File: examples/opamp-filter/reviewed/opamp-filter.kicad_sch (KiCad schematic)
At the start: 28 parts, among them J1 IN, J2 5V, J3 OUT, U1 MCP6001R, U2 MCP6001R

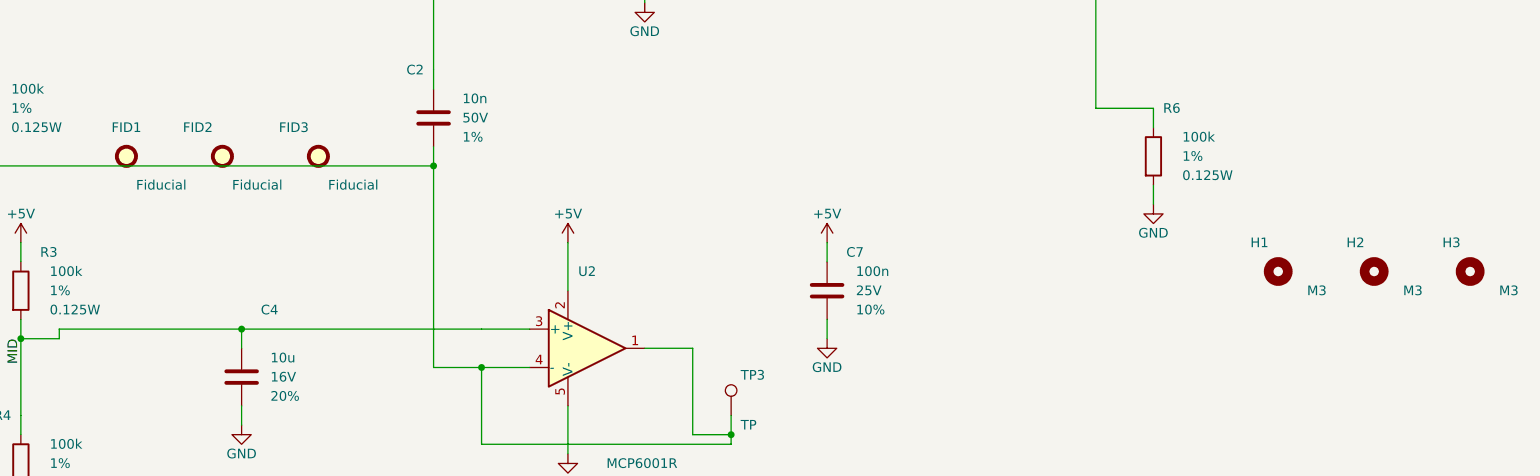
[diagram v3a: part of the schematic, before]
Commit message: Put the vias back where the copper moved, and let the fillets vote
The FPGA board came back from its re-route with two unconnected nets and
three dangling ends, and the cause was older than anything this round
added. The router hands back a via for every layer change; six passes
then reshape the copper - snapping to 45s, chamfering, spreading folds,
and now filleting - and none of them move the holes underneath. A joint
that slides a millimetre from its via is two loose ends and one broken
net, and `_unlooped` then swept the via away as orphaned, because it
kept a via only when a track ended on its exact coordinate.

Two fixes, both about what "connected" means. A via lives if kept copper
*touches* it, not if a coordinate matches. And a new `_joined` pass
re-derives the joints from the copper that actually got written: where a
net ends on two layers at one point with no via reaching it, one goes
back in. It reads the finished geometry, so it cannot drift the way six
separate passes carrying vias along with them would.

The same reasoning fixes two rules that had been measuring coordinates
rather than copper. `route.stub` matched a track end to a via's centre
exactly, and called a joint a stub whenever a reshaping pass had moved
it a quarter of a millimetre inside the very barrel it was connected to.
`route.width_step` walked a neck back to its pad and stopped at the
first width change - which, on a filleted board, is the teardrop, so
every escape's neck stopped being recognised as one.

While the three copies of the post-route pipeline were being edited for
the third time this session, they became one function. That is how
`_teardrops` had come to run on two of the three exits.

All five boards: DRC clean on both matrix versions, nothing unconnected.
Four pass their gates; the FPGA board is down to the two-layer bill it
has always had - four nets over plane cuts and one 88 degree corner.

Co-Authored-By: Claude Fable 5 <noreply@anthropic.com>
Claude-Session: https:/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
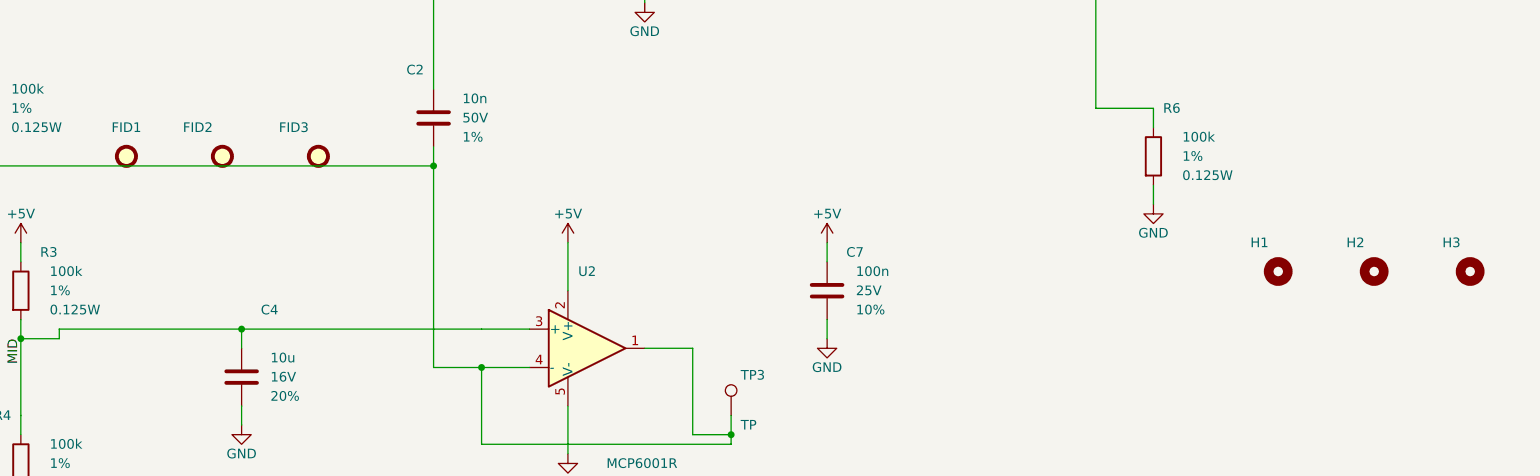
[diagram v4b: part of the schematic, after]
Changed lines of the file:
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@@
     (exclude_from_sim no) (in_bom no) (on_board yes) (dnp no)
     (property "Reference" "H1" (at 240.03 146.05 0) (effects (font (size 1.27 1.27)) (justify right)))
-    (property "Value" "M3" (at 245.11 152.4 0) (effects (font (size 1.27 1.27)) (justify left)))
+    (property "Value" "M3" (at 245.11 152.4 0) (effects (font (size 1.27 1.27)) (justify left) hide))
     (property "Footprint" "MountingHole:MountingHole_3.2mm_M3" (at 241.3 149.86 0) (effects (font (size 1.27 1.27)) hide))
     (property "Datasheet" "~" (at 241.3 149.86 0) (effects (font (size 1.27 1.27)) hide))
@@
     (exclude_from_sim no) (in_bom no) (on_board yes) (dnp no)
     (property "Reference" "H2" (at 252.73 146.05 0) (effects (font (size 1.27 1.27)) (justify right)))
-    (property "Value" "M3" (at 257.81 152.4 0) (effects (font (size 1.27 1.27)) (justify left)))
+    (property "Value" "M3" (at 257.81 152.4 0) (effects (font (size 1.27 1.27)) (justify left) hide))
     (property "Footprint" "MountingHole:MountingHole_3.2mm_M3" (at 254.0 149.86 0) (effects (font (size 1.27 1.27)) hide))
     (property "Datasheet" "~" (at 254.0 149.86 0) (effects (font (size 1.27 1.27)) hide))
@@
     (exclude_from_sim no) (in_bom no) (on_board yes) (dnp no)
     (property "Reference" "H3" (at 265.43 146.05 0) (effects (font (size 1.27 1.27)) (justify right)))
-    (property "Value" "M3" (at 270.51 152.4 0) (effects (font (size 1.27 1.27)) (justify left)))
+    (property "Value" "M3" (at 270.51 152.4 0) (effects (font (size 1.27 1.27)) (justify left) hide))
     (property "Footprint" "MountingHole:MountingHole_3.2mm_M3" (at 266.7 149.86 0) (effects (font (size 1.27 1.27)) hide))
     (property "Datasheet" "~" (at 266.7 149.86 0) (effects (font (size 1.27 1.27)) hide))
@@
     (exclude_from_sim no) (in_bom no) (on_board yes) (dnp no)
     (property "Reference" "FID1" (at 88.9 130.81 0) (effects (font (size 1.27 1.27))))
-    (property "Value" "Fiducial" (at 90.17 138.43 0) (effects (font (size 1.27 1.27)) (justify left)))
+    (property "Value" "Fiducial" (at 90.17 138.43 0) (effects (font (size 1.27 1.27)) (justify left) hide))
     (property "Footprint" "Fiducial:Fiducial_1mm_Mask2mm" (at 88.9 134.62 0) (effects (font (size 1.27 1.27)) hide))
     (property "Datasheet" "~" (at 88.9 134.62 0) (effects (font (size 1.27 1.27)) hide))
@@
     (exclude_from_sim no) (in_bom no) (on_board yes) (dnp no)
     (property "Reference" "FID2" (at 100.33 130.81 0) (effects (font (size 1.27 1.27)) (justify right)))
-    (property "Value" "Fiducial" (at 102.87 138.43 0) (effects (font (size 1.27 1.27)) (justify left)))
+    (property "Value" "Fiducial" (at 102.87 138.43 0) (effects (font (size 1.27 1.27)) (justify left) hide))
     (property "Footprint" "Fiducial:Fiducial_1mm_Mask2mm" (at 101.60000000000001 134.62 0) (effects (font (size 1.27 1.27)) hide))
     (property "Datasheet" "~" (at 101.60000000000001 134.62 0) (effects (font (size 1.27 1.27)) hide))
@@
     (exclude_from_sim no) (in_bom no) (on_board yes) (dnp no)
     (property "Reference" "FID3" (at 113.03 130.81 0) (effects (font (size 1.27 1.27)) (justify right)))
-    (property "Value" "Fiducial" (at 115.57 138.43 0) (effects (font (size 1.27 1.27)) (justify left)))
+    (property "Value" "Fiducial" (at 115.57 138.43 0) (effects (font (size 1.27 1.27)) (justify left) hide))
     (property "Footprint" "Fiducial:Fiducial_1mm_Mask2mm" (at 114.30000000000001 134.62 0) (effects (font (size 1.27 1.27)) hide))
     (property "Datasheet" "~" (at 114.30000000000001 134.62 0) (effects (font (size 1.27 1.27)) hide))

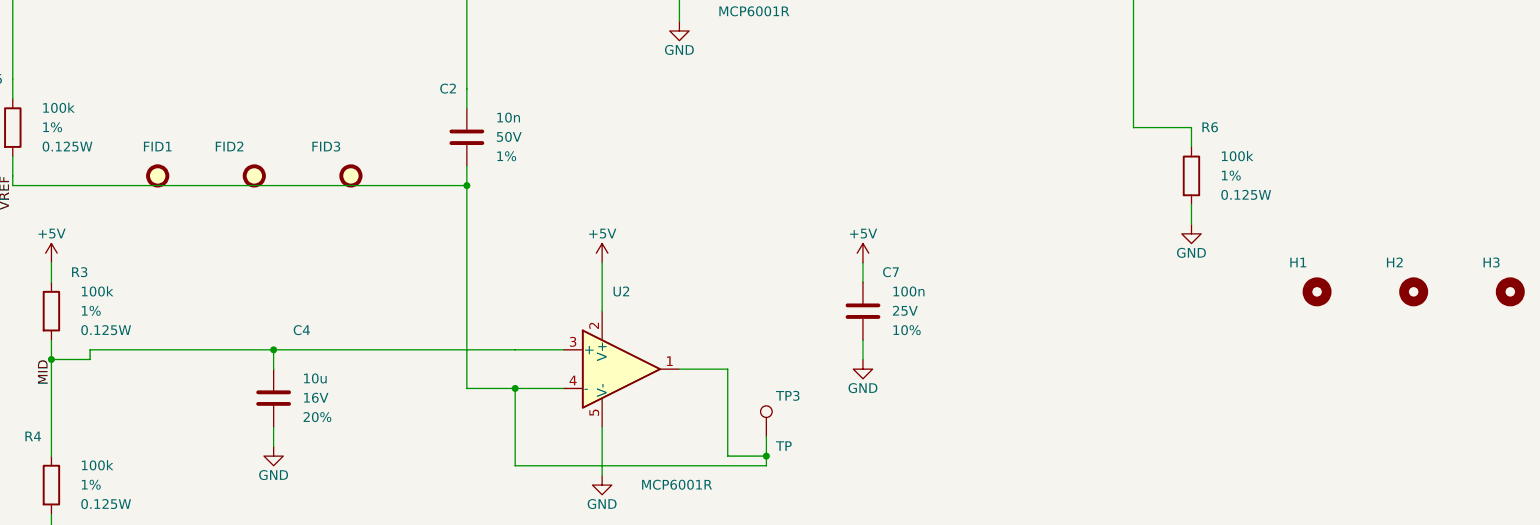
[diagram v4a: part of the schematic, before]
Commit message: Leave room for the screw, and print the ink where the board is
The screw holes were placed against the hole's own courtyard, which is the
drill plus a whisker - so on four of the five boards a hole sat inside a
connector's mating space, closest 0.42 mm. What goes through an M3 hole is a
pan head on a washer, seven millimetres of steel lying flat, and a connector
wants its shell, its wires and the fingers that fit them on top of that. The
spot search now keeps the fastener's own circle clear of every part body and
gives connectors CONNECTOR_ACCESS more, and three rules say so when a board
does not: mechanical.fastener_clearance, mechanical.connector_access and
mechanical.fastener_copper, all blocking for a generated design.

Silk was measured with a per-character advance of 0.78, and KiCad's stroke
font is proportional at 0.94 to 1.07. Everything downstream of that estimate
was placing ink where it did not fit: a legend across a capacitor's land, a
designator through the board's own name. `_text_extent` takes the top of the
measured range, adds the fab's clearance and is used by every silk placement.

Three placements also fell through to a position nobody chose. A designator
that found nothing kept its library offset, which for a part in a corner
points off the board; the board id took the first of eight fixed strips; a
legend took the least bad of six spots. All three are scored now, over
candidate sets wide enough to have an answer - and a pad-less footprint, which
is what a mounting hole is, is no longer skipped outright.

silk.off_board reports the case KiCad's own test cannot: ink that clears the
edge entirely is never printed, and DRC only measures ink that crosses it.

_unspiked redraws a corner tighter than a right angle as the elbow between its
neighbours - one diagonal, one straight, no step back to a heading the line
has already left. It is never longer than what it replaces.

All four fast boards: 0 errors, 0 warnings.

Co-Authored-By: Claude Fable 5 <no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
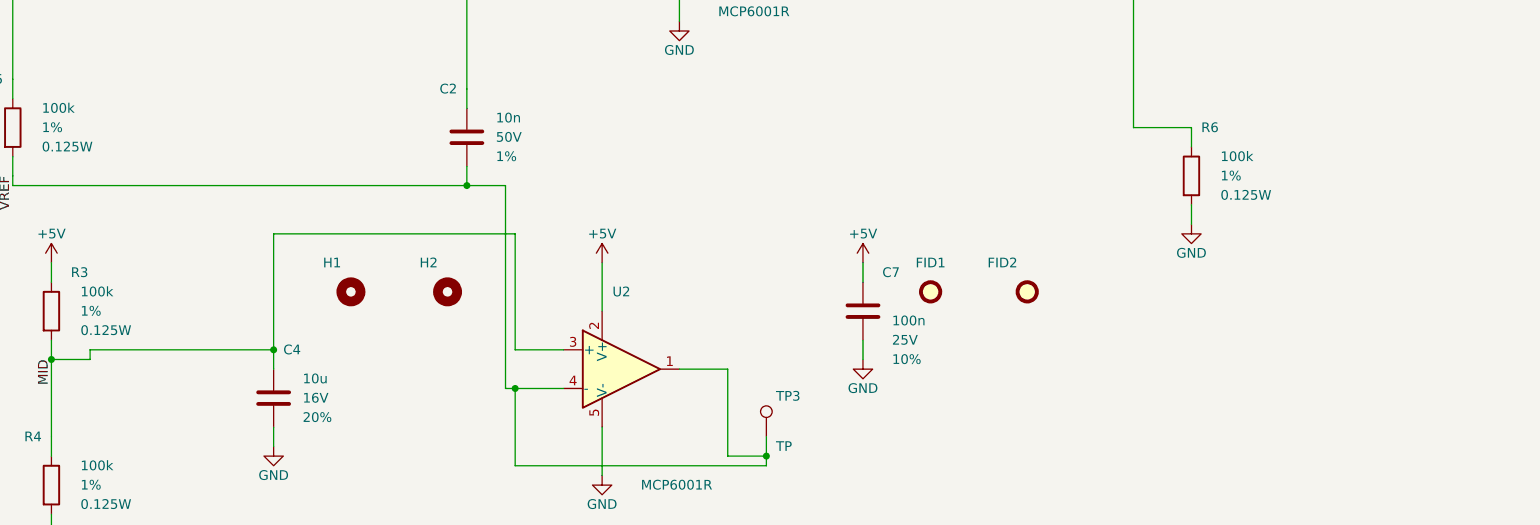
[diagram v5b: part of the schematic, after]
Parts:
- removed FID3: Fiducial, Fiducial:Fiducial_1mm_Mask2mm, symbol Mechanical:Fiducial
- removed H3: M3, MountingHole:MountingHole_3.2mm_M3, symbol Mechanical:MountingHole
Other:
- moved on the sheet: FID1, FID2, H1, H2

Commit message: Walk the whole edge for a screw hole, and land a joint on its own pad
The fastener clearance was right and the search was not: it slid along two
edges from each corner and gave up, so boards that had had four screw holes
came back with one. It now walks a ring round the board at the inset the
screw needs, taking the nearest free point to each corner - and only from
that corner's own quarter, because a search that asked for the nearest free
point anywhere put three of the four along one edge, each of them the nearest
thing to a different corner. A quarter with no room gives no screw: three
that hold the board flat beat four that hold one side.

A pin header asks for nothing above its courtyard - the socket that fits it
lands inside the outline the header already draws - while a screw terminal's
wires leave horizontally from its face. Treating the two alike is what left a
carrier lined with headers with two holes on one edge. Both the generator and
the rule now tell them apart by footprint.

_landed folds a via that sits beside a plated hole of its own net onto the
hole. The plating already joins the faces, so the via bought nothing and cost
hole-to-hole: two drills a millimetre apart leave 0.15 mm of laminate at a
0.25 mm rule, which is what DRC reported on the opamp board.

The fillets move to the end of the pipeline. A taper is built against the end
of a run, and _landed moves ends, so a teardrop laid before it pointed at
where the run used to stop - a nought-degree corner in the angle rule.

buck-5v, motor-driver, pico-carrier, opamp-filter: 0 errors, 0 warnings.

Co-Authored-By: Claude Fable 5 <noreply@anthropic.com>
Claude-Session: https://claude.ai/code/session_01DUj7Ltu92tWg159mCSacwY
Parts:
- added FID3: Fiducial, Fiducial:Fiducial_1mm_Mask2mm, symbol Mechanical:Fiducial
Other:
- moved on the sheet: FID1, FID2
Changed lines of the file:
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@@
     (exclude_from_sim no) (in_bom yes) (on_board yes) (dnp no)
     (property "Reference" "C7" (at 184.15 147.32 0) (effects (font (size 1.27 1.27)) (justify left)))
-    (property "Value" "100n" (at 185.42 153.67 0) (effects (font (size 1.27 1.27)) (justify left)))
+    (property "Value" "100n" (at 185.42 149.86 0) (effects (font (size 1.27 1.27)) (justify left)))
     (property "Footprint" "Capacitor_SMD:C_0805_2012Metric" (at 181.61 152.4 0) (effects (font (size 1.27 1.27)) hide))
     (property "Datasheet" "https://product.samsungsem.com/mlcc/CL21B104KBCNNNC.do" (at 181.61 152.4 0) (effects (font (size 1.27 1.27)) hide))
-    (property "Voltage" "25V" (at 185.42 156.21 0) (effects (font (size 1.27 1.27)) (justify left)))
-    (property "Tolerance" "10%" (at 185.42 158.75 0) (effects (font (size 1.27 1.27)) (justify left)))
+    (property "Voltage" "25V" (at 185.42 152.4 0) (effects (font (size 1.27 1.27)) (justify left)))
+    (property "Tolerance" "10%" (at 185.42 154.94 0) (effects (font (size 1.27 1.27)) (justify left)))
     (property "MPN" "CL21B104KBCNNNC" (at 181.61 152.4 0) (effects (font (size 1.27 1.27)) hide))
     (property "Manufacturer" "Samsung" (at 181.61 152.4 0) (effects (font (size 1.27 1.27)) hide))
@@
     (instances (project "opamp-filter" (path "/efb028ab-a5b5-5d27-b654-08a8ba6b5d9d" (reference "H2") (unit 1))))
   )
-  (symbol (lib_id "Mechanical:Fiducial") (at 190.5 149.86 0.0) (unit 1)
+  (symbol (lib_id "Mechanical:Fiducial") (at 241.3 149.86 0.0) (unit 1)
     (exclude_from_sim no) (in_bom no) (on_board yes) (dnp no)
-    (property "Reference" "FID1" (at 190.5 146.05 0) (effects (font (size 1.27 1.27))))
-    (property "Value" "Fiducial" (at 194.31 152.4 0) (effects (font (size 1.27 1.27)) (justify left) hide))
-    (property "Footprint" "Fiducial:Fiducial_1mm_Mask2mm" (at 190.5 149.86 0) (effects (font (size 1.27 1.27)) hide))
-    (property "Datasheet" "~" (at 190.5 149.86 0) (effects (font (size 1.27 1.27)) hide))
-    (property "MPN" "n/a" (at 190.5 149.86 0) (effects (font (size 1.27 1.27)) hide))
-    (property "Manufacturer" "n/a" (at 190.5 149.86 0) (effects (font (size 1.27 1.27)) hide))
+    (property "Reference" "FID1" (at 240.03 146.05 0) (effects (font (size 1.27 1.27)) (justify right)))
+    (property "Value" "Fiducial" (at 245.11 152.4 0) (effects (font (size 1.27 1.27)) (justify left) hide))
+    (property "Footprint" "Fiducial:Fiducial_1mm_Mask2mm" (at 241.3 149.86 0) (effects (font (size 1.27 1.27)) hide))
+    (property "Datasheet" "~" (at 241.3 149.86 0) (effects (font (size 1.27 1.27)) hide))
+    (property "MPN" "n/a" (at 241.3 149.86 0) (effects (font (size 1.27 1.27)) hide))
+    (property "Manufacturer" "n/a" (at 241.3 149.86 0) (effects (font (size 1.27 1.27)) hide))
     (instances (project "opamp-filter" (path "/efb028ab-a5b5-5d27-b654-08a8ba6b5d9d" (reference "FID1") (unit 1))))
   )
-  (symbol (lib_id "Mechanical:Fiducial") (at 203.2 149.86 0.0) (unit 1)
+  (symbol (lib_id "Mechanical:Fiducial") (at 254.0 149.86 0.0) (unit 1)
     (exclude_from_sim no) (in_bom no) (on_board yes) (dnp no)
-    (property "Reference" "FID2" (at 201.93 146.05 0) (effects (font (size 1.27 1.27)) (justify right)))
-    (property "Value" "Fiducial" (at 207.01 152.4 0) (effects (font (size 1.27 1.27)) (justify left) hide))
-    (property "Footprint" "Fiducial:Fiducial_1mm_Mask2mm" (at 203.2 149.86 0) (effects (font (size 1.27 1.27)) hide))
-    (property "Datasheet" "~" (at 203.2 149.86 0) (effects (font (size 1.27 1.27)) hide))
-    (property "MPN" "n/a" (at 203.2 149.86 0) (effects (font (size 1.27 1.27)) hide))
-    (property "Manufacturer" "n/a" (at 203.2 149.86 0) (effects (font (size 1.27 1.27)) hide))
+    (property "Reference" "FID2" (at 252.73 146.05 0) (effects (font (size 1.27 1.27)) (justify right)))
+    (property "Value" "Fiducial" (at 257.81 152.4 0) (effects (font (size 1.27 1.27)) (justify left) hide))
+    (property "Footprint" "Fiducial:Fiducial_1mm_Mask2mm" (at 254.0 149.86 0) (effects (font (size 1.27 1.27)) hide))
+    (property "Datasheet" "~" (at 254.0 149.86 0) (effects (font (size 1.27 1.27)) hide))
+    (property "MPN" "n/a" (at 254.0 149.86 0) (effects (font (size 1.27 1.27)) hide))
+    (property "Manufacturer" "n/a" (at 254.0 149.86 0) (effects (font (size 1.27 1.27)) hide))
     (instances (project "opamp-filter" (path "/efb028ab-a5b5-5d27-b654-08a8ba6b5d9d" (reference "FID2") (unit 1))))
   )
+  (symbol (lib_id "Mechanical:Fiducial") (at 266.7 149.86 0.0) (unit 1)
+    (exclude_from_sim no) (in_bom no) (on_board yes) (dnp no)
+    (property "Reference" "FID3" (at 265.43 146.05 0) (effects (font (size 1.27 1.27)) (justify right)))
+    (property "Value" "Fiducial" (at 270.51 152.4 0) (effects (font (size 1.27 1.27)) (justify left) hide))
+    (property "Footprint" "Fiducial:Fiducial_1mm_Mask2mm" (at 266.7 149.86 0) (effects (font (size 1.27 1.27)) hide))
+    (property "Datasheet" "~" (at 266.7 149.86 0) (effects (font (size 1.27 1.27)) hide))
+    (property "MPN" "n/a" (at 266.7 149.86 0) (effects (font (size 1.27 1.27)) hide))
+    (property "Manufacturer" "n/a" (at 266.7 149.86 0) (effects (font (size 1.27 1.27)) hide))
+    (instances (project "opamp-filter" (path "/efb028ab-a5b5-5d27-b654-08a8ba6b5d9d" (reference "FID3") (unit 1))))
+  )
   (wire (pts (xy 38.1 102.87) (xy 45.72 102.87)) (stroke (width 0) (type default)))
